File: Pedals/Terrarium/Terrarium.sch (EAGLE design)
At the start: 43 parts, among them IC1 TL072CP, IC2 LM78L05

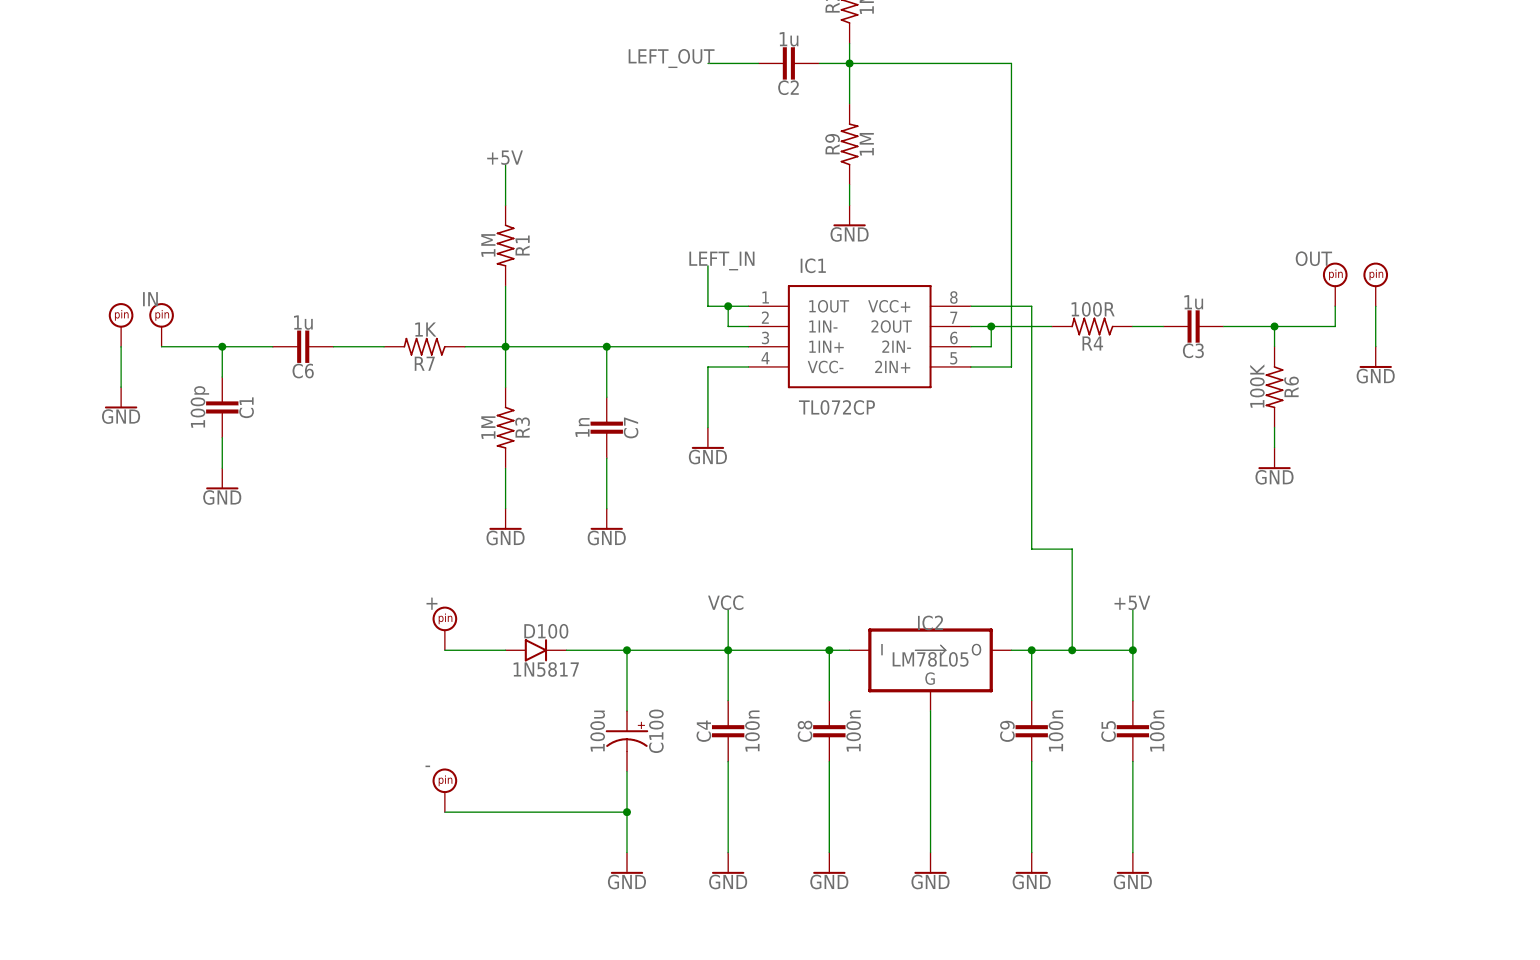
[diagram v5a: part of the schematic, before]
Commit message: Add true bypass
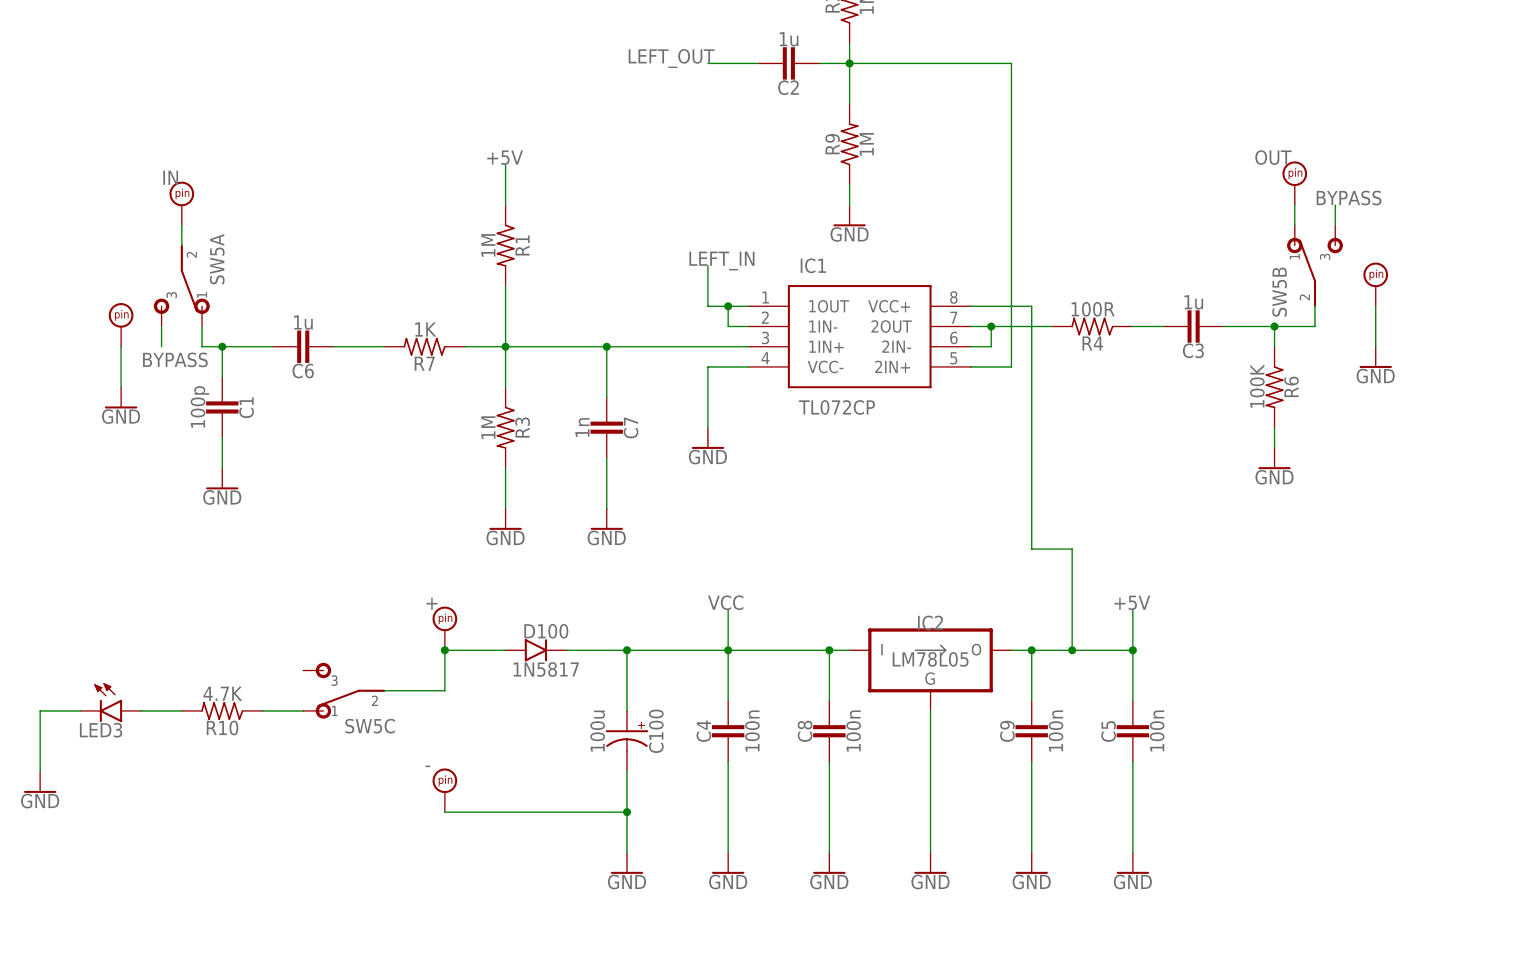
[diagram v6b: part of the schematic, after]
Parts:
- added LED3: LED.3, diodes:LED.3
- added R10: 4.7K, resistors:R.3B
- added SW5: 3PDTTOGGLE, switches:3PDTTOGGLE
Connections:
- new net BYPASS: SW5A.3, SW5B.3
- new net N$13: IN.P$1, SW5A.2
- new net N$18: OUT.P$1, SW5B.1
- new net N$19: R10.1, SW5C.1
- new net N$20: LED3.A, R10.2
- net GND: now also LED3.C
- net N$11: now also SW5B.2; no longer OUT.P$1
- net N$12: now also SW5A.1; no longer IN.P$1
- net N$9: now also SW5C.2
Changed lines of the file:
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@@
 <part name="SW4" library="switches" deviceset="SPDT" device=".1"/>
 <part name="IC2" library="regulators" deviceset="LM78L05" device=""/>
+<part name="SW5" library="switches" deviceset="3PDT" device="TOGGLE"/>
+<part name="R10" library="resistors" deviceset="R" device=".3B" value="4.7K"/>
+<part name="LED3" library="diodes" deviceset="LED" device=".3"/>
+<part name="GND31" library="SparkFun-PowerSymbols" library_urn="urn:adsk.eagle:library:530" deviceset="GND" device=""/>
 </parts>
 <sheets>
@@
 <attribute name="VALUE" x="-43.18" y="27.686" size="1.778" layer="96" align="top-center"/>
 </instance>
-<instance part="OUT" gate="G$1" x="-35.56" y="48.26" smashed="yes">
-<attribute name="NM" x="-40.64" y="53.34" size="1.778" layer="96"/>
+<instance part="OUT" gate="G$1" x="-40.64" y="60.96" smashed="yes">
+<attribute name="NM" x="-45.72" y="66.04" size="1.778" layer="96"/>
 </instance>
 <instance part="OUT_GND" gate="G$1" x="-30.48" y="48.26" smashed="yes">
@@
 <attribute name="VALUE" x="-30.48" y="40.386" size="1.778" layer="96" align="top-center"/>
 </instance>
-<instance part="IN" gate="G$1" x="-182.88" y="43.18" smashed="yes">
-<attribute name="NM" x="-185.42" y="48.26" size="1.778" layer="96"/>
+<instance part="IN" gate="G$1" x="-180.34" y="58.42" smashed="yes">
+<attribute name="NM" x="-182.88" y="63.5" size="1.778" layer="96"/>
 </instance>
 <instance part="IN_GND" gate="G$1" x="-187.96" y="43.18" smashed="yes">
@@
 <attribute name="NAME" x="-86.36" y="8.509" size="1.778" layer="95" align="center"/>
 <attribute name="VALUE" x="-86.36" y="3.937" size="1.778" layer="96" align="center"/>
+</instance>
+<instance part="SW5" gate="A" x="-180.34" y="50.8" smashed="yes" rot="R180">
+<attribute name="NAME" x="-175.895" y="54.102" size="1.778" layer="95" rot="R270" align="center"/>
+</instance>
+<instance part="SW5" gate="B" x="-38.1" y="53.34" smashed="yes">
+<attribute name="NAME" x="-42.545" y="50.038" size="1.778" layer="95" rot="R90" align="center"/>
+</instance>
+<instance part="SW5" gate="C" x="-160.02" y="0" smashed="yes" rot="R90">
+<attribute name="NAME" x="-156.718" y="-4.445" size="1.778" layer="95" rot="R180" align="center"/>
+</instance>
+<instance part="R10" gate="G$1" x="-175.26" y="-2.54" smashed="yes" rot="R180">
+<attribute name="NAME" x="-175.26" y="-4.6736" size="1.778" layer="95" rot="R180" align="center"/>
+<attribute name="VALUE" x="-175.26" y="-0.381" size="1.778" layer="96" rot="R180" align="center"/>
+</instance>
+<instance part="LED3" gate="G$1" x="-190.5" y="-2.54" smashed="yes">
+<attribute name="NAME" x="-190.5" y="-4.953" size="1.778" layer="95" align="center"/>
+</instance>
+<instance part="GND31" gate="1" x="-198.12" y="-12.7" smashed="yes">
+<attribute name="VALUE" x="-198.12" y="-12.954" size="1.778" layer="96" align="top-center"/>
 </instance>
 </instances>
@@
 <wire x1="-86.36" y1="-2.54" x2="-86.36" y2="-20.32" width="0.1524" layer="91"/>
 </segment>
+<segment>
+<pinref part="LED3" gate="G$1" pin="C"/>
+<wire x1="-193.04" y1="-2.54" x2="-198.12" y2="-2.54" width="0.1524" layer="91"/>
+<pinref part="GND31" gate="1" pin="GND"/>
+<wire x1="-198.12" y1="-2.54" x2="-198.12" y2="-10.16" width="0.1524" layer="91"/>
+</segment>
 </net>
 <net name="3V3_A" class="0">
@@
 <pinref part="D100" gate="G$1" pin="A"/>
 <wire x1="-147.32" y1="5.08" x2="-139.7" y2="5.08" width="0.1524" layer="91"/>
+<wire x1="-147.32" y1="5.08" x2="-147.32" y2="0" width="0.1524" layer="91"/>
+<junction x="-147.32" y="5.08"/>
+<pinref part="SW5" gate="C" pin="2"/>
+<wire x1="-147.32" y1="0" x2="-154.94" y2="0" width="0.1524" layer="91"/>
 </segment>
 </net>
@@
 <pinref part="R6" gate="G$1" pin="1"/>
 <wire x1="-43.18" y1="45.72" x2="-43.18" y2="43.18" width="0.1524" layer="91"/>
-<wire x1="-43.18" y1="45.72" x2="-35.56" y2="45.72" width="0.1524" layer="91"/>
+<pinref part="C3" gate="G$1" pin="2"/>
+<wire x1="-43.18" y1="45.72" x2="-38.1" y2="45.72" width="0.1524" layer="91"/>
 <junction x="-43.18" y="45.72"/>
-<pinref part="OUT" gate="G$1" pin="P$1"/>
-<wire x1="-35.56" y1="45.72" x2="-35.56" y2="48.26" width="0.1524" layer="91"/>
-<pinref part="C3" gate="G$1" pin="2"/>
+<pinref part="SW5" gate="B" pin="2"/>
+<wire x1="-38.1" y1="45.72" x2="-38.1" y2="48.26" width="0.1524" layer="91"/>
 </segment>
 </net>
 <net name="N$12" class="0">
 <segment>
-<pinref part="IN" gate="G$1" pin="P$1"/>
-<wire x1="-182.88" y1="43.18" x2="-175.26" y2="43.18" width="0.1524" layer="91"/>
 <wire x1="-175.26" y1="43.18" x2="-168.91" y2="43.18" width="0.1524" layer="91"/>
 <wire x1="-175.26" y1="39.37" x2="-175.26" y2="43.18" width="0.1524" layer="91"/>
-<junction x="-175.26" y="43.18"/>
 <pinref part="C1" gate="G$1" pin="2"/>
 <pinref part="C6" gate="G$1" pin="1"/>
+<pinref part="SW5" gate="A" pin="1"/>
+<wire x1="-177.8" y1="45.72" x2="-177.8" y2="43.18" width="0.1524" layer="91"/>
+<wire x1="-177.8" y1="43.18" x2="-175.26" y2="43.18" width="0.1524" layer="91"/>
+<junction x="-175.26" y="43.18"/>
 </segment>
 </net>
@@
 </segment>
 </net>
+<net name="N$13" class="0">
+<segment>
+<pinref part="IN" gate="G$1" pin="P$1"/>
+<pinref part="SW5" gate="A" pin="2"/>
+<wire x1="-180.34" y1="58.42" x2="-180.34" y2="55.88" width="0.1524" layer="91"/>
+</segment>
+</net>
+<net name="N$18" class="0">
+<segment>
+<pinref part="SW5" gate="B" pin="1"/>
+<pinref part="OUT" gate="G$1" pin="P$1"/>
+<wire x1="-40.64" y1="58.42" x2="-40.64" y2="60.96" width="0.1524" layer="91"/>
+</segment>
+</net>
+<net name="BYPASS" class="0">
+<segment>
+<pinref part="SW5" gate="B" pin="3"/>
+<wire x1="-35.56" y1="58.42" x2="-35.56" y2="60.96" width="0.1524" layer="91"/>
+<label x="-38.1" y="60.96" size="1.778" layer="95"/>
+</segment>
+<segment>
+<pinref part="SW5" gate="A" pin="3"/>
+<wire x1="-182.88" y1="45.72" x2="-182.88" y2="43.18" width="0.1524" layer="91"/>
+<label x="-185.42" y="40.64" size="1.778" layer="95"/>
+</segment>
+</net>
+<net name="N$19" class="0">
+<segment>
+<pinref part="R10" gate="G$1" pin="1"/>
+<pinref part="SW5" gate="C" pin="1"/>
+<wire x1="-170.18" y1="-2.54" x2="-165.1" y2="-2.54" width="0.1524" layer="91"/>
+</segment>
+</net>
+<net name="N$20" class="0">
+<segment>
+<pinref part="R10" gate="G$1" pin="2"/>
+<pinref part="LED3" gate="G$1" pin="A"/>
+<wire x1="-180.34" y1="-2.54" x2="-185.42" y2="-2.54" width="0.1524" layer="91"/>
+</segment>
+</net>

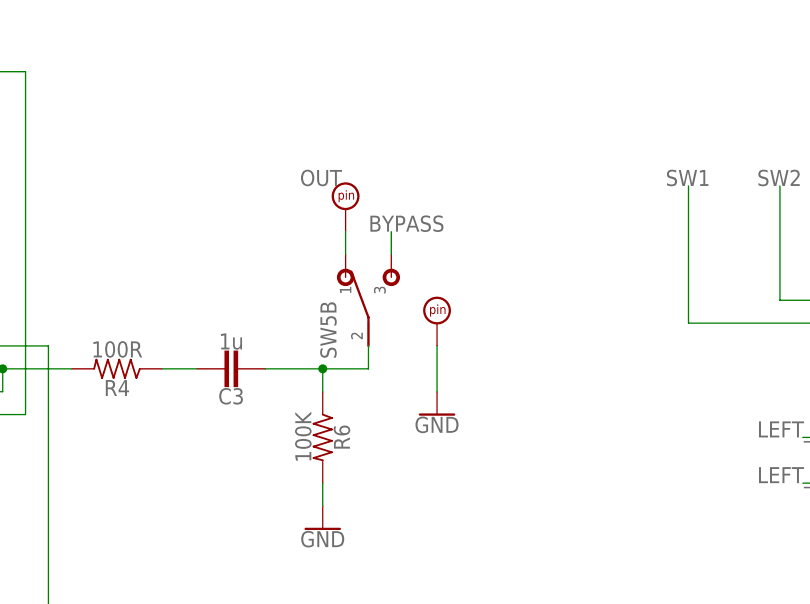
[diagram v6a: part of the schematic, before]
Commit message: Fix true bypass circuit on Terrarium
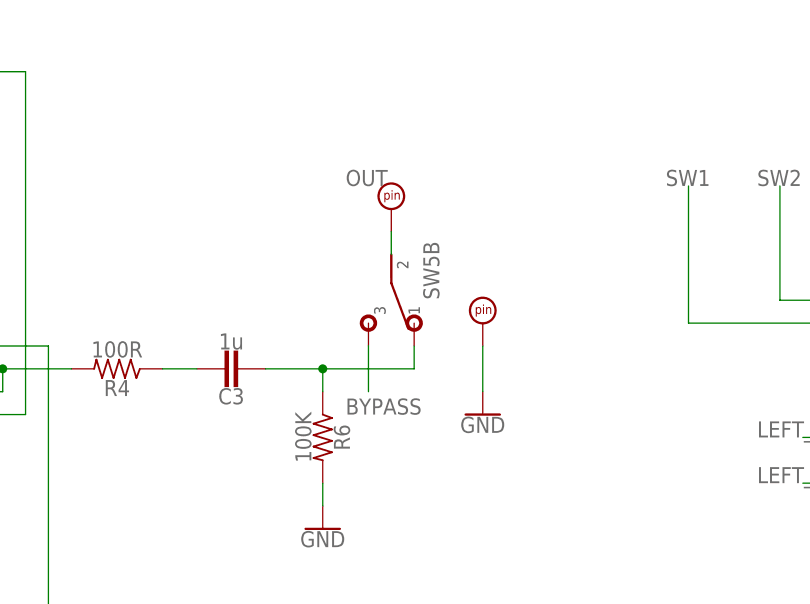
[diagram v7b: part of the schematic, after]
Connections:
- removed net N$18: OUT.P$1, SW5B.1
- new net N$21: OUT.P$1, SW5B.2
- net N$11: now also SW5B.1; no longer SW5B.2
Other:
- moved on the sheet: SW5B
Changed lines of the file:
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@@
 <attribute name="VALUE" x="-43.18" y="27.686" size="1.778" layer="96" align="top-center"/>
 </instance>
-<instance part="OUT" gate="G$1" x="-40.64" y="60.96" smashed="yes">
-<attribute name="NM" x="-45.72" y="66.04" size="1.778" layer="96"/>
-</instance>
-<instance part="OUT_GND" gate="G$1" x="-30.48" y="48.26" smashed="yes">
-<attribute name="NM" x="-30.48" y="48.26" size="1.778" layer="96" display="off"/>
-</instance>
-<instance part="GND26" gate="1" x="-30.48" y="40.64" smashed="yes">
-<attribute name="VALUE" x="-30.48" y="40.386" size="1.778" layer="96" align="top-center"/>
+<instance part="OUT" gate="G$1" x="-35.56" y="60.96" smashed="yes">
+<attribute name="NM" x="-40.64" y="66.04" size="1.778" layer="96"/>
+</instance>
+<instance part="OUT_GND" gate="G$1" x="-25.4" y="48.26" smashed="yes">
+<attribute name="NM" x="-25.4" y="48.26" size="1.778" layer="96" display="off"/>
+</instance>
+<instance part="GND26" gate="1" x="-25.4" y="40.64" smashed="yes">
+<attribute name="VALUE" x="-25.4" y="40.386" size="1.778" layer="96" align="top-center"/>
 </instance>
 <instance part="IN" gate="G$1" x="-180.34" y="58.42" smashed="yes">
@@
 <attribute name="NAME" x="-175.895" y="54.102" size="1.778" layer="95" rot="R270" align="center"/>
 </instance>
-<instance part="SW5" gate="B" x="-38.1" y="53.34" smashed="yes">
-<attribute name="NAME" x="-42.545" y="50.038" size="1.778" layer="95" rot="R90" align="center"/>
+<instance part="SW5" gate="B" x="-35.56" y="53.34" smashed="yes" rot="R180">
+<attribute name="NAME" x="-31.115" y="56.642" size="1.778" layer="95" rot="R270" align="center"/>
 </instance>
 <instance part="SW5" gate="C" x="-160.02" y="0" smashed="yes" rot="R90">
@@
 <pinref part="OUT_GND" gate="G$1" pin="P$1"/>
 <pinref part="GND26" gate="1" pin="GND"/>
-<wire x1="-30.48" y1="48.26" x2="-30.48" y2="43.18" width="0.1524" layer="91"/>
+<wire x1="-25.4" y1="48.26" x2="-25.4" y2="43.18" width="0.1524" layer="91"/>
 </segment>
 <segment>
@@
 <wire x1="-43.18" y1="45.72" x2="-43.18" y2="43.18" width="0.1524" layer="91"/>
 <pinref part="C3" gate="G$1" pin="2"/>
-<wire x1="-43.18" y1="45.72" x2="-38.1" y2="45.72" width="0.1524" layer="91"/>
 <junction x="-43.18" y="45.72"/>
-<pinref part="SW5" gate="B" pin="2"/>
-<wire x1="-38.1" y1="45.72" x2="-38.1" y2="48.26" width="0.1524" layer="91"/>
+<pinref part="SW5" gate="B" pin="1"/>
+<wire x1="-43.18" y1="45.72" x2="-33.02" y2="45.72" width="0.1524" layer="91"/>
+<wire x1="-33.02" y1="45.72" x2="-33.02" y2="48.26" width="0.1524" layer="91"/>
 </segment>
 </net>
@@
 </segment>
 </net>
-<net name="N$18" class="0">
-<segment>
-<pinref part="SW5" gate="B" pin="1"/>
-<pinref part="OUT" gate="G$1" pin="P$1"/>
-<wire x1="-40.64" y1="58.42" x2="-40.64" y2="60.96" width="0.1524" layer="91"/>
-</segment>
-</net>
 <net name="BYPASS" class="0">
-<segment>
-<pinref part="SW5" gate="B" pin="3"/>
-<wire x1="-35.56" y1="58.42" x2="-35.56" y2="60.96" width="0.1524" layer="91"/>
-<label x="-38.1" y="60.96" size="1.778" layer="95"/>
-</segment>
 <segment>
 <pinref part="SW5" gate="A" pin="3"/>
@@
 <label x="-185.42" y="40.64" size="1.778" layer="95"/>
 </segment>
+<segment>
+<pinref part="SW5" gate="B" pin="3"/>
+<wire x1="-38.1" y1="48.26" x2="-38.1" y2="43.18" width="0.1524" layer="91"/>
+<label x="-40.64" y="40.64" size="1.778" layer="95"/>
+</segment>
 </net>
 <net name="N$19" class="0">
@@
 </segment>
 </net>
+<net name="N$21" class="0">
+<segment>
+<pinref part="OUT" gate="G$1" pin="P$1"/>
+<pinref part="SW5" gate="B" pin="2"/>
+<wire x1="-35.56" y1="60.96" x2="-35.56" y2="58.42" width="0.1524" layer="91"/>
+</segment>
+</net>
